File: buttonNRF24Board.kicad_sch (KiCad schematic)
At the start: 22 parts, among them J1 INTERFACE, U1 NRF24L01, X1 16MHz

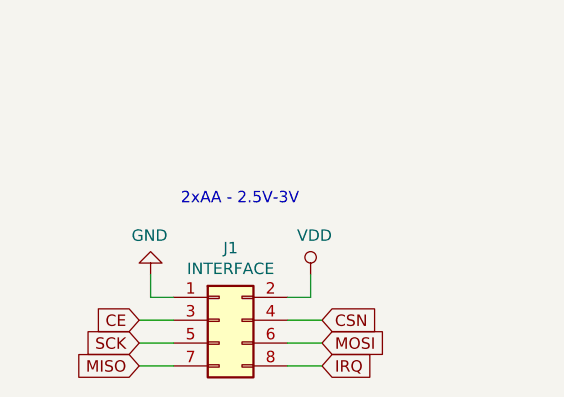
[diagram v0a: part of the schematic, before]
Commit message: Tweaking board shape and traces
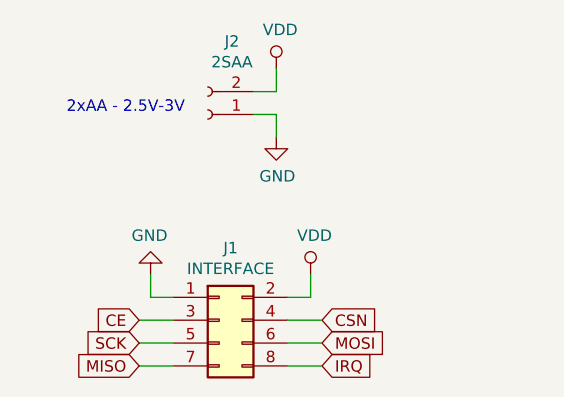
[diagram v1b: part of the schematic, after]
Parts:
- added J2: 2SAA, Connector_PinHeader_2.54mm:PinHeader_1x02_P2.54mm_Vertical, symbol Connector:Conn_01x02_Female
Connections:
- net EP: now also J2.1 (Pin_1)
- net VDD: now also J2.2 (Pin_2)
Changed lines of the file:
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@@
+    (stroke (width 0) (type solid) (color 0 0 0 0))
+  )
+  (wire (pts (xy 113.03 57.15) (xy 113.03 59.69))
+    (stroke (width 0) (type solid) (color 0 0 0 0))
+  )
+  (wire (pts (xy 113.03 59.69) (xy 110.49 59.69))
+    (stroke (width 0) (type solid) (color 0 0 0 0))
+  )
+  (wire (pts (xy 113.03 62.23) (xy 110.49 62.23))
+    (stroke (width 0) (type solid) (color 0 0 0 0))
+  )
+  (wire (pts (xy 113.03 64.77) (xy 113.03 62.23))
     (stroke (width 0) (type solid) (color 0 0 0 0))
   )
@@
     (stroke (width 0) (type solid) (color 0 0 0 0))
   )
-  (text "2xAA - 2.5V-3V" (at 115.57 72.39 180)
+  (text "2xAA - 2.5V-3V" (at 102.87 62.23 180)
     (effects (font (size 1.27 1.27)) (justify right bottom))
   )
@@
     )
   )
+  (symbol (lib_id "power:VDD") (at 113.03 57.15 0) (unit 1)
+    (in_bom yes) (on_board yes)
+    (property "Reference" "#PWR014" (id 0) (at 113.03 60.96 0)
+      (effects (font (size 1.27 1.27)) hide)
+    )
+    (property "Value" "VDD" (id 1) (at 113.4618 52.8256 0))
+    (property "Footprint" "" (id 2) (at 113.03 57.15 0)
+      (effects (font (size 1.27 1.27)) hide)
+    )
+    (property "Datasheet" "" (id 3) (at 113.03 57.15 0)
+      (effects (font (size 1.27 1.27)) hide)
+    )
+  )
   (symbol (lib_id "power:VDD") (at 116.84 80.01 0) (unit 1)
     (in_bom yes) (on_board yes)
@@
     )
   )
+  (symbol (lib_id "power:GND") (at 113.03 64.77 0) (unit 1)
+    (in_bom yes) (on_board yes)
+    (property "Reference" "#PWR015" (id 0) (at 113.03 71.12 0)
+      (effects (font (size 1.27 1.27)) hide)
+    )
+    (property "Value" "GND" (id 1) (at 113.1443 69.0944 0))
+    (property "Footprint" "" (id 2) (at 113.03 64.77 0)
+      (effects (font (size 1.27 1.27)) hide)
+    )
+    (property "Datasheet" "" (id 3) (at 113.03 64.77 0)
+      (effects (font (size 1.27 1.27)) hide)
+    )
+  )
   (symbol (lib_id "power:GND") (at 137.16 139.7 0) (unit 1)
     (in_bom yes) (on_board yes)
@@
     )
     (property "Datasheet" "~" (id 3) (at 209.55 120.65 0)
+      (effects (font (size 1.27 1.27)) hide)
+    )
+  )
+  (symbol (lib_id "Connector:Conn_01x02_Female") (at 105.41 62.23 180) (unit 1)
+    (in_bom yes) (on_board yes)
+    (property "Reference" "J2" (id 0) (at 108.1024 54.1082 0))
+    (property "Value" "2SAA" (id 1) (at 108.1024 56.4134 0))
+    (property "Footprint" "Connector_PinHeader_2.54mm:PinHeader_1x02_P2.54mm_Vertical" (id 2) (at 105.41 62.23 0)
+      (effects (font (size 1.27 1.27)) hide)
+    )
+    (property "Datasheet" "~" (id 3) (at 105.41 62.23 0)
       (effects (font (size 1.27 1.27)) hide)
     )
@@
       (reference "#PWR013") (unit 1) (value "GND") (footprint "")
     )
+    (path "/f24aaa94-f397-47dc-8c58-d0bec5518ca2"
+      (reference "#PWR014") (unit 1) (value "VDD") (footprint "")
+    )
+    (path "/45d6913c-e38e-4ff3-b2db-05127c1ea3ba"
+      (reference "#PWR015") (unit 1) (value "GND") (footprint "")
+    )
     (path "/97d0c502-ad0d-447b-a52d-02a366a9d6c6"
       (reference "AE1") (unit 1) (value "Antenna") (footprint "RF_Antenna:Texas_SWRA117D_2.4GHz_Left")
@@
       (reference "J1") (unit 1) (value "INTERFACE") (footprint "Connector_PinHeader_2.54mm:PinHeader_2x04_P2.54mm_Vertical")
     )
+    (path "/3cb65299-2673-4744-bef1-42d5ef1a8e9b"
+      (reference "J2") (unit 1) (value "2SAA") (footprint "Connector_PinHeader_2.54mm:PinHeader_1x02_P2.54mm_Vertical")
+    )
     (path "/deccef2c-7679-4b2d-add4-7eb4a05f7fc9"
